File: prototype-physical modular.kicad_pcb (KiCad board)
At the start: 2 copper layers, 100 x 164 mm, 183 parts, among them CON1 BARREL_JACK, CON2 SD_Card, IC1 ATMEGA2560-A, P1 POWER, P10 PC, P11 CONN_UART, P12 PJ, P13 PD, P15 PH, P16 PF, P17 SD_PINS, P18 3VI2C, P19 PIGPIO, P20 MIDI_IN, P21 MIDI_OUT, P22 BUSTI, P23 BUSTO, P3 SPI, P7 PA, Q1 BSS138, Q2 BSS138, Q3 BSS138, Q4 BSS138, Q5 BSS138, Q6 BSS138, SW1 SW_PUSH, SW10 SW_PUSH, SW11 SW_PUSH, SW12 SW_PUSH, SW13 SW_PUSH, SW14 SW_PUSH, SW2 ROTARY_ENCODER_SWITCH, SW3 SW_PUSH, SW4 SW_PUSH, SW5 SW_PUSH, SW6 SW_PUSH, SW7 SW_PUSH, SW8 SW_PUSH, SW9 SW_PUSH, U1 NCP1117ST50T3G, U2 6N138, Y1 16MHz

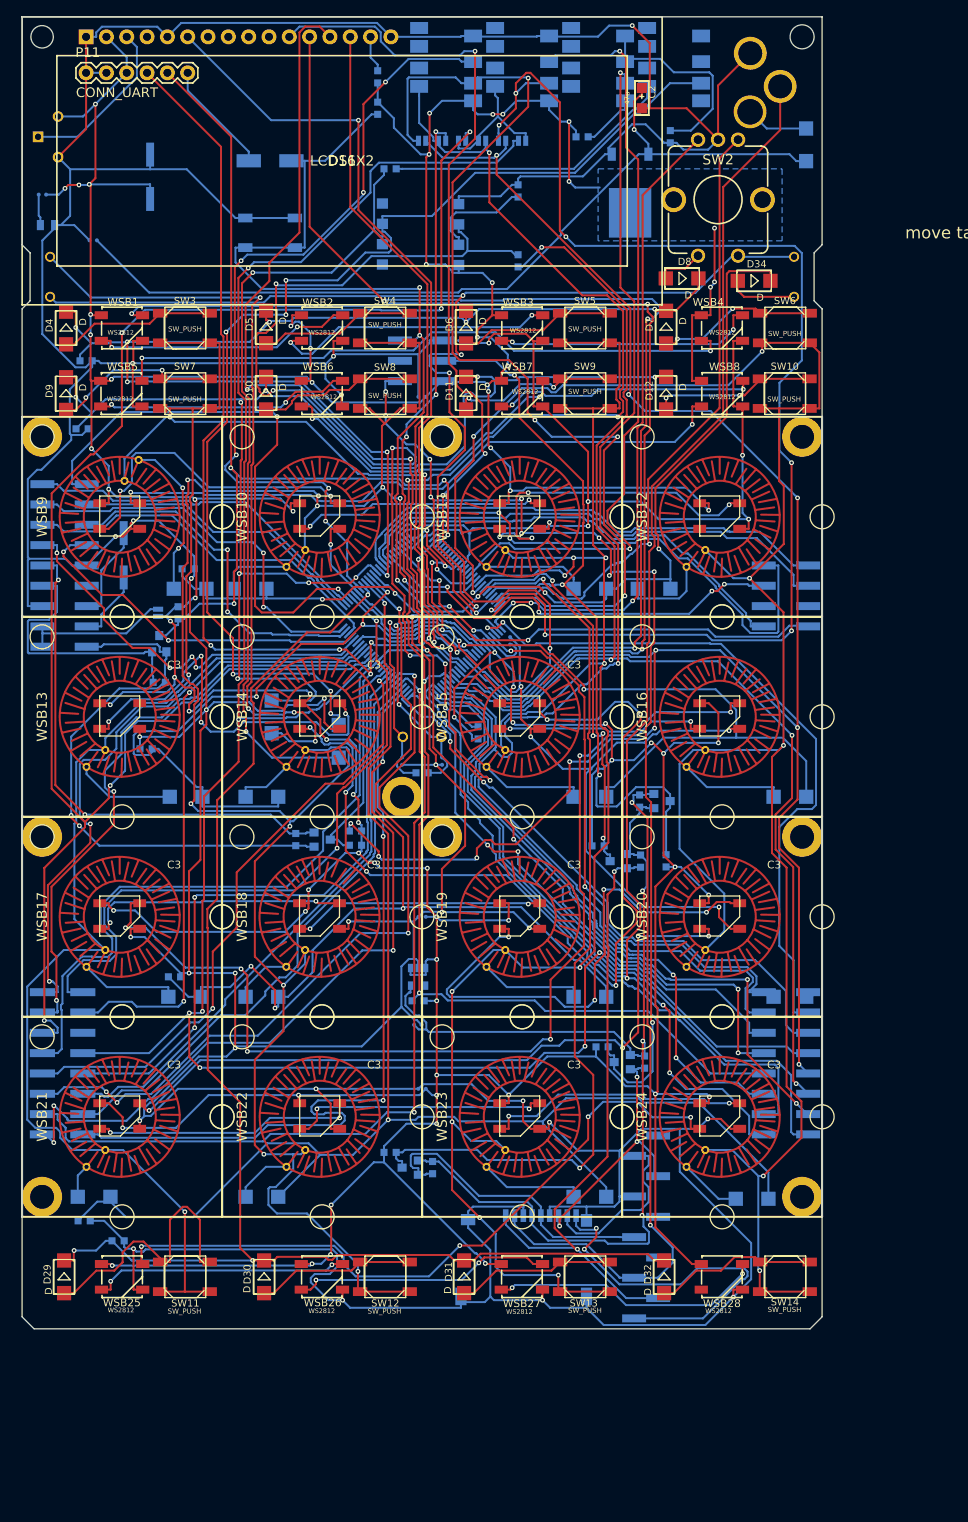
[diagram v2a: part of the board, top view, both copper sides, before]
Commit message: fix sd card pins were catastrophically wrong still figuring out layout
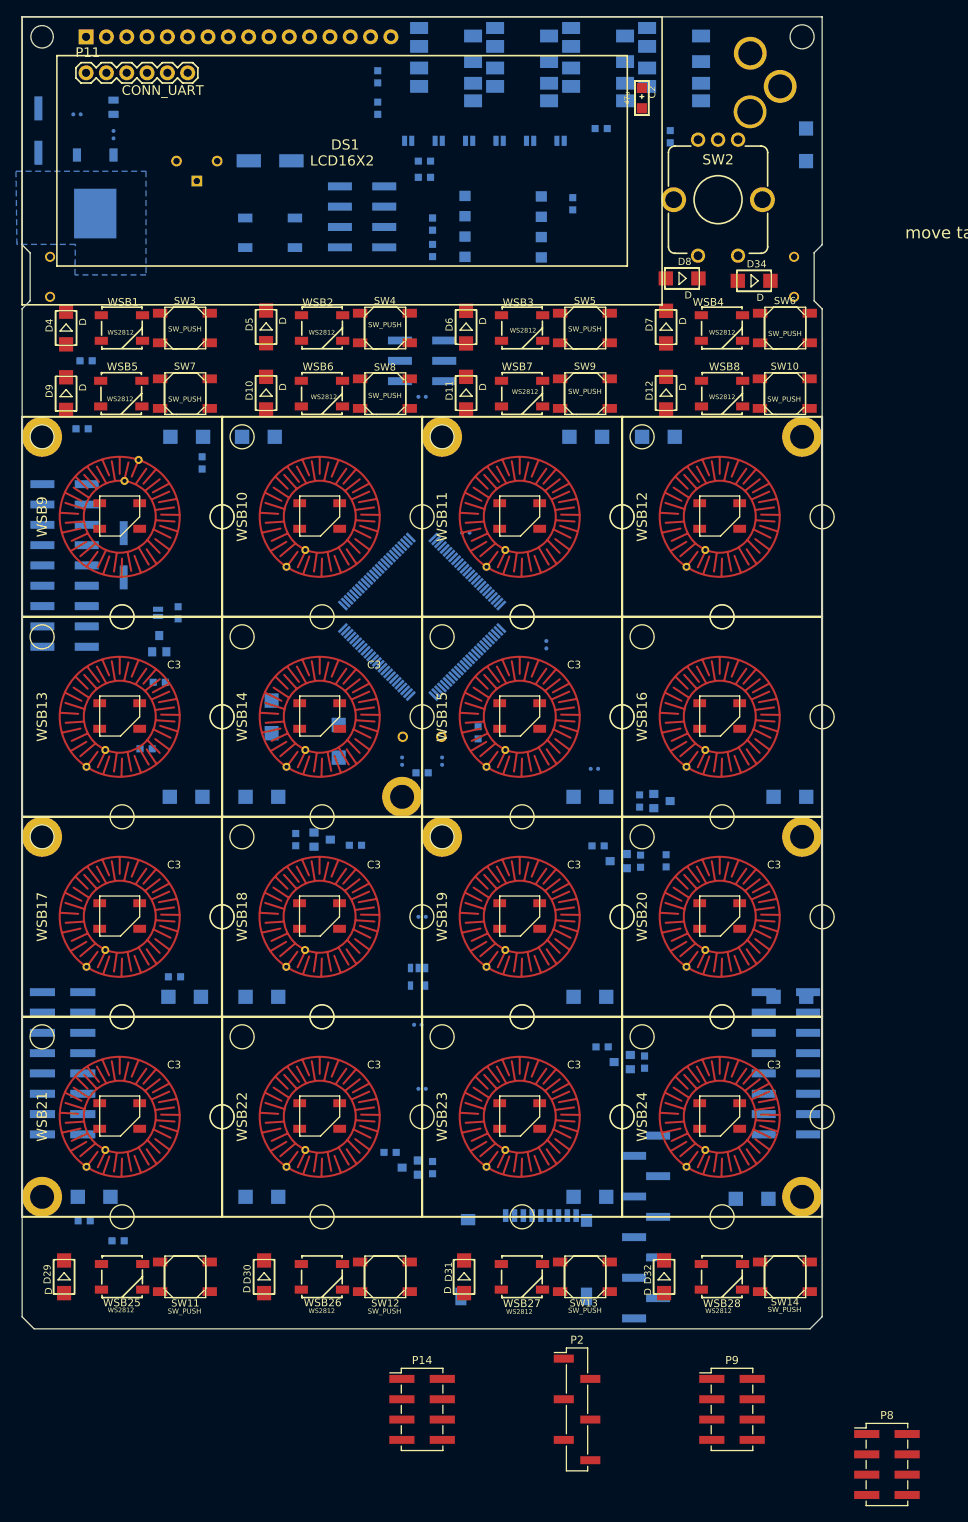
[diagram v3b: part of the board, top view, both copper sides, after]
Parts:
- added P14: PE, Pin_Headers:Pin_Header_Straight_2x04_Pitch2.54mm_SMD, F.Cu at (50.0, 174.1)
- added P2: FTDI, Pin_Headers:Pin_Header_Straight_1x06_Pitch2.54mm_SMD_Pin1Left, F.Cu at (69.4, 174.1)
- added P8: PL, Pin_Headers:Pin_Header_Straight_2x04_Pitch2.54mm_SMD, F.Cu at (108.1, 181.0)
- added P9: PB, Pin_Headers:Pin_Header_Straight_2x04_Pitch2.54mm_SMD, F.Cu at (88.7, 174.1)
- CON2: value SD_Card -> SD_Card_SEEEDOPL
- IC1: footprint SparkFun-DigitalIC:TQFP100 -> SeeedOPL-IC:TQFP100-0.5-14X14MM
- moved R10 105.0 mm to (50.3, 18.0)
- moved R9 82.2 mm to (50.3, 20.1)
- moved P16 71.1 mm to (42.5, 25.0)
- moved U1 66.9 mm to (9.14, 22.1)
- moved R4 23.2 mm to (68.8, 23.4), turned to 180 degrees
- moved RV1 20.6 mm to (21.8, 20.5), turned to 0 degrees
- moved D14 19.0 mm to (29.5, 52.5)
- moved D16 19.0 mm to (79.5, 52.5), turned to 180 degrees
- moved D15 19.0 mm to (70.5, 52.5)
- moved D13 19.0 mm to (20.6, 52.5)
- moved D2 16.9 mm to (11.4, 11.3), turned to 90 degrees
- moved P1 15.1 mm to (2.03, 14.2)
- moved C1 13.5 mm to (11.4, 14.7), turned to 0 degrees
- moved R27 13.4 mm to (22.5, 55.8), turned to 0 degrees
- moved R5 13.0 mm to (51.3, 29.2), turned to 0 degrees
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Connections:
- CON2 pad 1: /3VSD_CS -> /SD_DAT2
- CON2 pad 2: /3vSPI_MOSI -> /3VSD_CS
- CON2 pad 3: GND -> /3vSPI_MOSI
- CON2 pad 9: /SD_DAT2 -> /SD_CD
- CON2 pad G1: GND -> (no net)
- CON2 pad G2: GND -> (no net)
- CON2 pad G3: GND -> (no net)
- CON2 pad G4: GND -> (no net)
- P17 pad 2: /SD_DAT1 -> /SD_CD
- P17 pad 3: /3vSPI_MISO -> /SD_DAT1
- P17 pad 4: GND -> /3vSPI_MISO
- P17 pad 5: +3V3 -> GND
- P17 pad 7: (no net) -> +3V3
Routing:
- net GND: track 1122.6 -> 0.00 mm, vias 39 -> 0
- net +5V: track 897.1 -> 0.00 mm, vias 80 -> 0
- net /BUS_COM: track 277.6 -> 0.00 mm, vias 7 -> 0
- net /TX3: track 275.9 -> 0.00 mm, vias 7 -> 0
- net /MUXAX3: track 267.8 -> 0.00 mm, vias 7 -> 0
- net /SCL: track 263.0 -> 0.00 mm, vias 11 -> 0
- net /MUXAX1: track 253.3 -> 0.00 mm, vias 11 -> 0
- net /MUXAX0: track 236.3 -> 0.00 mm, vias 5 -> 0
- net /MUXAX2: track 223.9 -> 0.00 mm, vias 9 -> 0
- net Net-(IC1-Pad65): track 212.5 -> 0.00 mm, vias 5 -> 0
- net /POWER_IS: track 202.4 -> 0.00 mm, vias 3 -> 0
- net /MUXBX5: track 194.4 -> 0.00 mm, vias 2 -> 0
- net /MIDI_OUT_TX: track 180.3 -> 0.00 mm, vias 4 -> 0
- net /MUXBX6: track 176.7 -> 0.00 mm, vias 3 -> 0
- net /MUXBX1: track 172.4 -> 0.00 mm, vias 9 -> 0
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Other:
- board text added: "I2C pullups"

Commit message: more layout, inclusion of enclosure design
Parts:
- removed P13: PD, Pin_Headers:Pin_Header_Straight_2x04_Pitch2.54mm_SMD
- removed P14: PE, Pin_Headers:Pin_Header_Straight_2x04_Pitch2.54mm_SMD
- removed P17: SD_PINS, Pin_Headers:Pin_Header_Straight_1x10_Pitch2.54mm_SMD_Pin1Left
- removed P2: FTDI, Pin_Headers:Pin_Header_Straight_1x06_Pitch2.54mm_SMD_Pin1Left
- removed P8: PL, Pin_Headers:Pin_Header_Straight_2x04_Pitch2.54mm_SMD
- removed P9: PB, Pin_Headers:Pin_Header_Straight_2x04_Pitch2.54mm_SMD
- moved R6 69.9 mm to (59.7, 19.7), turned to 90 degrees
- moved D3 68.7 mm to (69.2, 28.6), turned to 90 degrees
- moved P7 48.3 mm to (5.31, 110.5)
- moved R5 3.64 mm to (49.5, 26.0)
- moved R24 2.77 mm to (52.1, 28.6), turned to 180 degrees
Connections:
- CON2 pad G4: (no net) -> GND
- IC1 pad 47: Net-(IC1-Pad47) -> /SD_CD

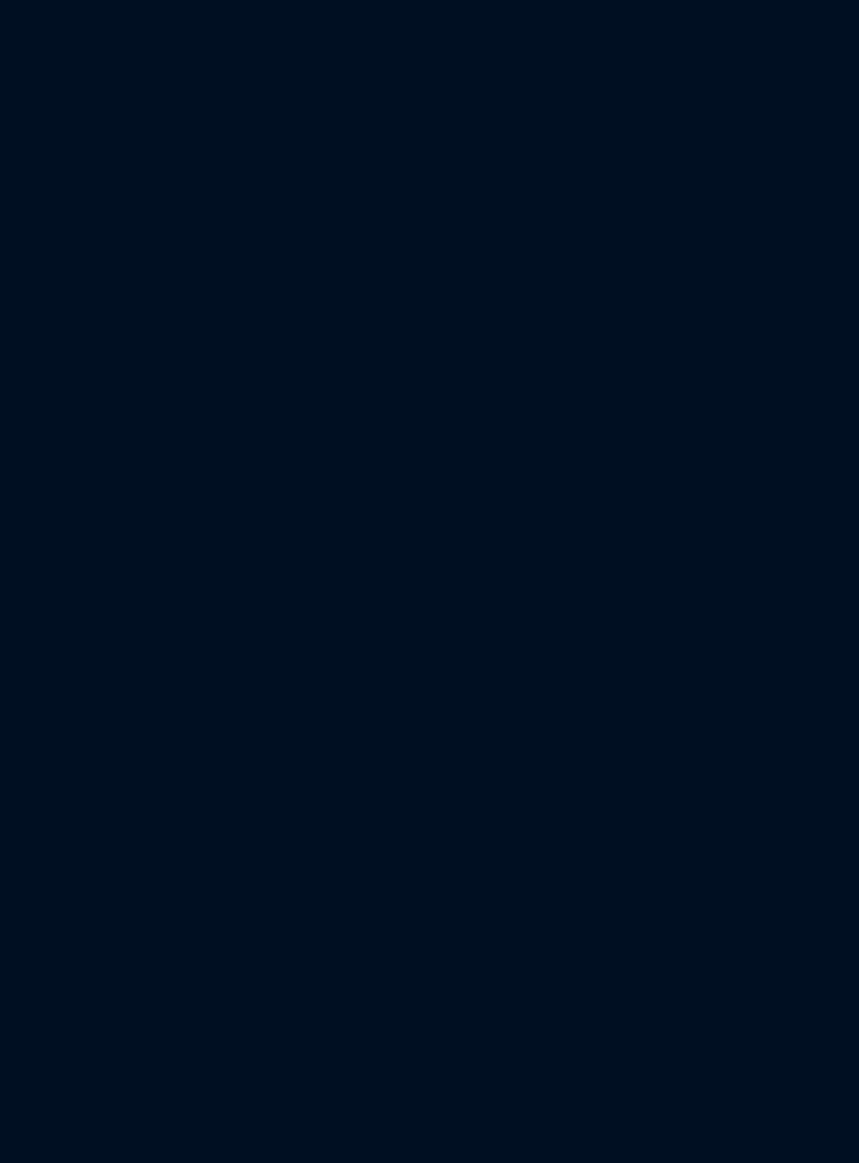
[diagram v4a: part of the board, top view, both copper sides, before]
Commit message: fix wrong midi jack plug
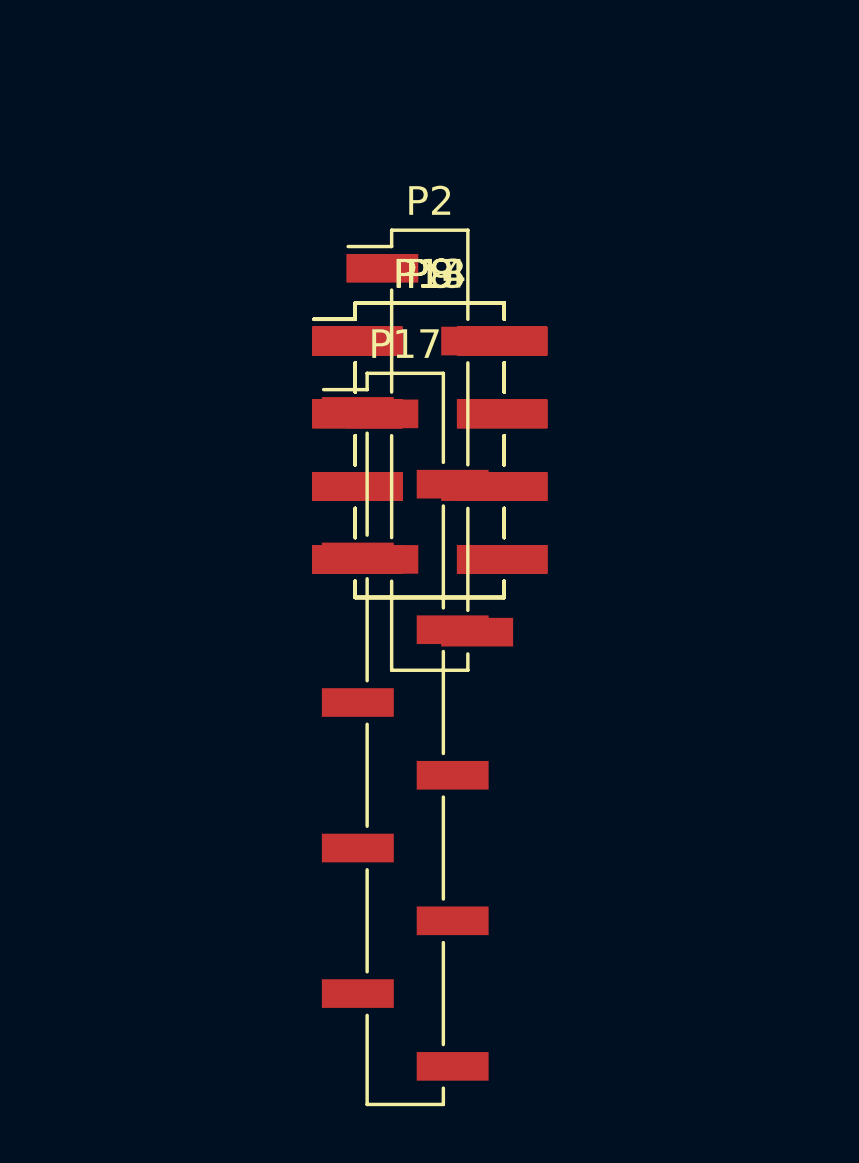
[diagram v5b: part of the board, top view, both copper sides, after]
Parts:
- added P13: PD, Pin_Headers:Pin_Header_Straight_2x04_Pitch2.54mm_SMD, F.Cu at (50.0, 196.9)
- added P14: PE, Pin_Headers:Pin_Header_Straight_2x04_Pitch2.54mm_SMD, F.Cu at (50.0, 196.9)
- added P17: SD_PINS, Pin_Headers:Pin_Header_Straight_1x10_Pitch2.54mm_SMD_Pin1Left, F.Cu at (49.1, 207.0)
- added P2: FTDI, Pin_Headers:Pin_Header_Straight_1x06_Pitch2.54mm_SMD_Pin1Left, F.Cu at (50.0, 196.9)
- added P8: PL, Pin_Headers:Pin_Header_Straight_2x04_Pitch2.54mm_SMD, F.Cu at (50.0, 196.9)
- added P9: PB, Pin_Headers:Pin_Header_Straight_2x04_Pitch2.54mm_SMD, F.Cu at (50.0, 196.9)
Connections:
- P21 pad 4: (no net) -> Net-(P21-Pad4)
- P21 pad 8: Net-(P21-Pad8) -> (no net)
- R2 pad 2: Net-(P21-Pad8) -> Net-(P21-Pad4)
- R3 pad 1: GND -> Net-(P21-Pad1)
- R3 pad 2: Net-(P21-Pad1) -> GND

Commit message: -
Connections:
- P22 pad 2: /BUSTI_CONN -> /BUS_COM
- P22 pad 4: /BUS_COM -> +5V
- P22 pad 6: (no net) -> /BUSTI_CONN
- P22 pad 8: +5V -> (no net)
- P23 pad 2: /BUSTO_CONN -> /BUS_COM_B
- P23 pad 4: /BUS_COM_B -> +5V
- P23 pad 6: (no net) -> /BUSTO_CONN
- P23 pad 8: +5V -> (no net)
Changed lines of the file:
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@@
       (net 2 GND))
     (pad 2 smd rect (at 7.0993 -3.37312 180) (size 2.2479 1.59766) (layers B.Cu B.Paste B.Mask)
-      (net 128 /BUSTI_CONN))
+      (net 71 /BUS_COM))
     (pad 3 smd rect (at 9.79932 -3.37312 180) (size 2.2479 1.59766) (layers B.Cu B.Paste B.Mask)
       (net 133 /BUS_TI))
     (pad 4 smd rect (at 10.1981 3.37312 180) (size 2.2479 1.59766) (layers B.Cu B.Paste B.Mask)
-      (net 71 /BUS_COM))
+      (net 1 +5V))
     (pad 5 smd rect (at 2.89814 3.37312 180) (size 2.2479 1.4986) (layers B.Cu B.Paste B.Mask))
-    (pad 6 smd rect (at 5.19938 3.37312 180) (size 2.2479 1.59766) (layers B.Cu B.Paste B.Mask))
+    (pad 6 smd rect (at 5.19938 3.37312 180) (size 2.2479 1.59766) (layers B.Cu B.Paste B.Mask)
+      (net 128 /BUSTI_CONN))
     (pad 7 smd rect (at 7.8994 3.37312 180) (size 2.2479 1.59766) (layers B.Cu B.Paste B.Mask))
-    (pad 8 smd rect (at 11.99896 -3.37312 180) (size 2.2479 1.59766) (layers B.Cu B.Paste B.Mask)
-      (net 1 +5V))
+    (pad 8 smd rect (at 11.99896 -3.37312 180) (size 2.2479 1.59766) (layers B.Cu B.Paste B.Mask))
   )
   (module SeeedOPL-Connector:AUDIO8P-SMD-3.5-14.5X6.1X4.0MM (layer B.Cu)
@@
       (net 2 GND))
     (pad 2 smd rect (at 7.0993 -3.37312 180) (size 2.2479 1.59766) (layers B.Cu B.Paste B.Mask)
-      (net 127 /BUSTO_CONN))
+      (net 129 /BUS_COM_B))
     (pad 3 smd rect (at 9.79932 -3.37312 180) (size 2.2479 1.59766) (layers B.Cu B.Paste B.Mask)
       (net 132 /BUS_TO))
     (pad 4 smd rect (at 10.1981 3.37312 180) (size 2.2479 1.59766) (layers B.Cu B.Paste B.Mask)
-      (net 129 /BUS_COM_B))
+      (net 1 +5V))
     (pad 5 smd rect (at 2.89814 3.37312 180) (size 2.2479 1.4986) (layers B.Cu B.Paste B.Mask))
-    (pad 6 smd rect (at 5.19938 3.37312 180) (size 2.2479 1.59766) (layers B.Cu B.Paste B.Mask))
+    (pad 6 smd rect (at 5.19938 3.37312 180) (size 2.2479 1.59766) (layers B.Cu B.Paste B.Mask)
+      (net 127 /BUSTO_CONN))
     (pad 7 smd rect (at 7.8994 3.37312 180) (size 2.2479 1.59766) (layers B.Cu B.Paste B.Mask))
-    (pad 8 smd rect (at 11.99896 -3.37312 180) (size 2.2479 1.59766) (layers B.Cu B.Paste B.Mask)
-      (net 1 +5V))
+    (pad 8 smd rect (at 11.99896 -3.37312 180) (size 2.2479 1.59766) (layers B.Cu B.Paste B.Mask))
   )
   (module SeeedOPL-Resistor:R0603 (layer B.Cu)
